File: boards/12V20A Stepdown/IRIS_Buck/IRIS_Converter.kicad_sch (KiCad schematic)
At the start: 27 parts, among them J1 TB005-762-02BE, J2 TB005-762-02BE, Q1 CSD17571Q2, Q2 CSD16340Q3, U1 LM25145RGYR

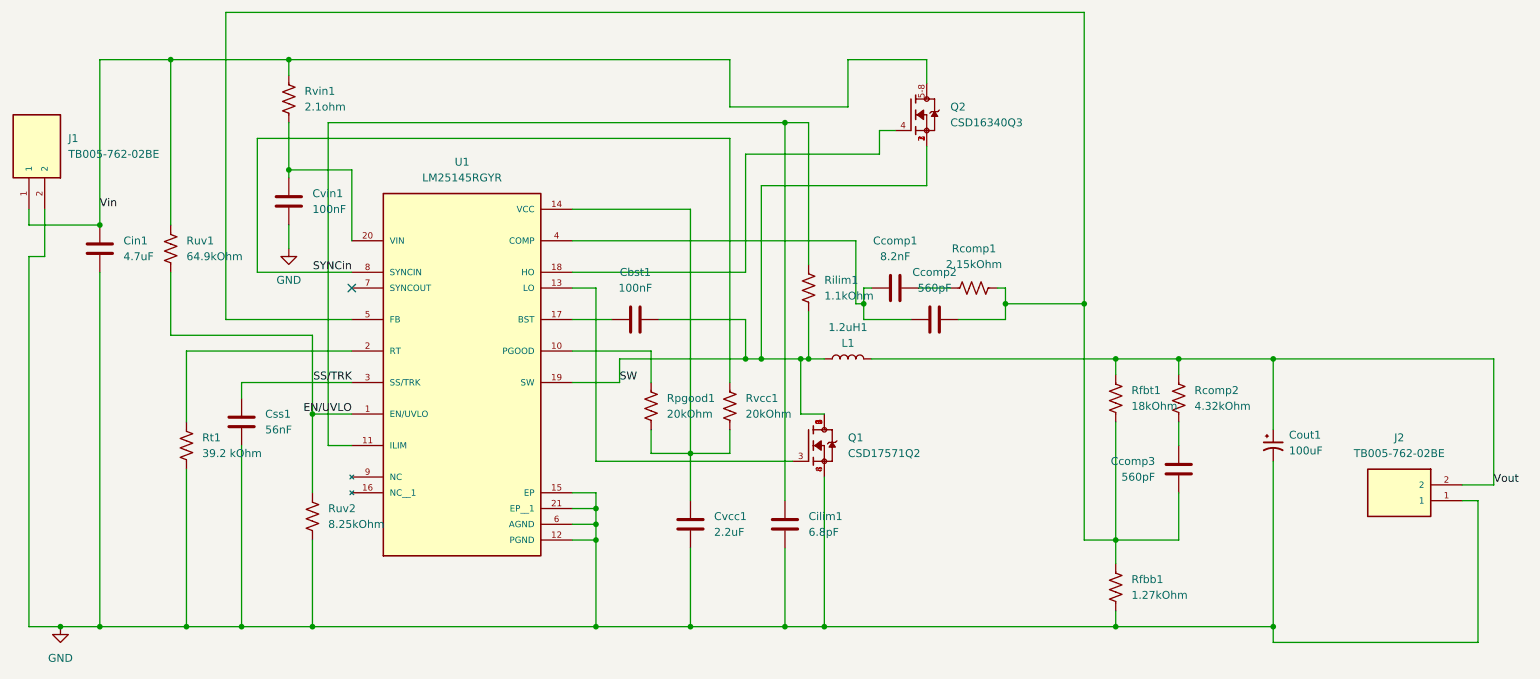
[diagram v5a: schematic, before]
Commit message: 10a stepdown and 20a stepdown update
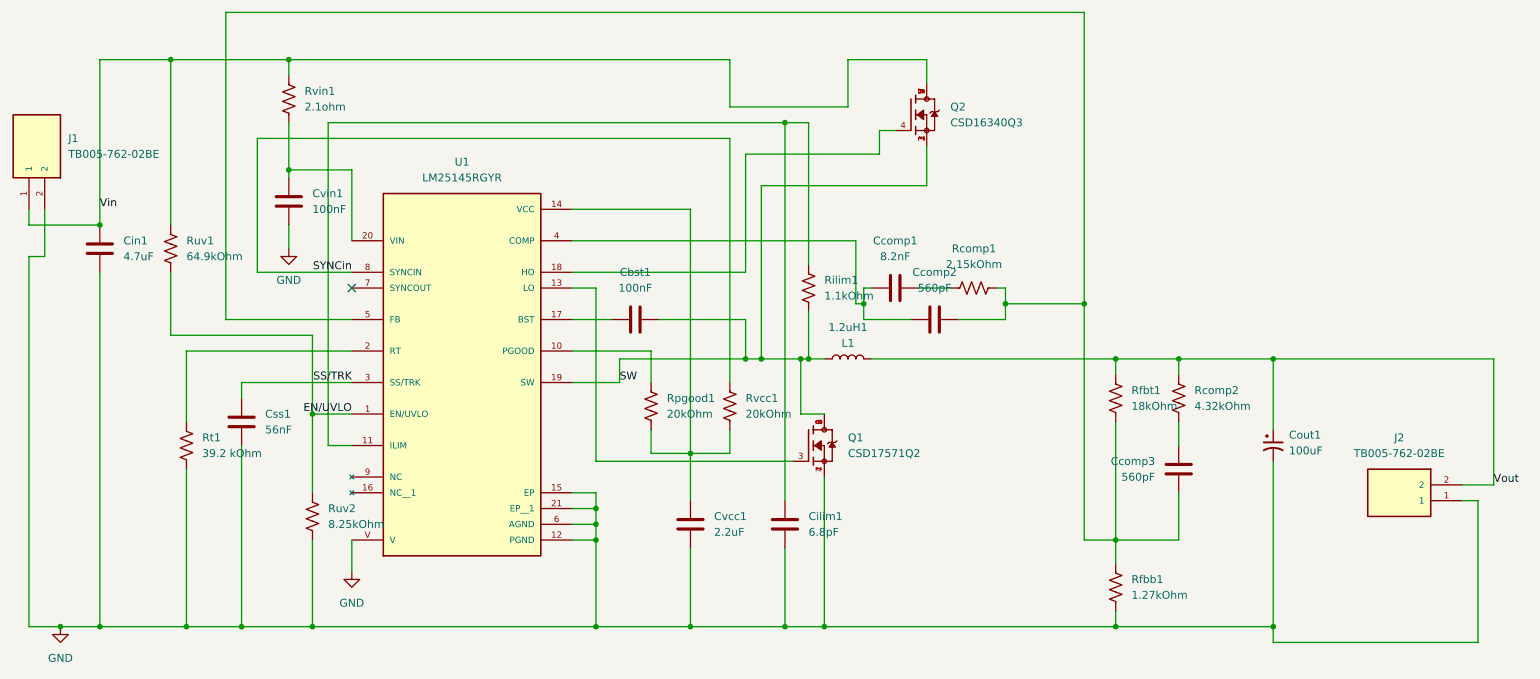
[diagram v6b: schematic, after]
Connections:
- net GND: now also Q1.7, U1.V; no longer Q1.8
- net SW: now also Q1.8; no longer Q1.7
- net Vin: now also Q2.5, Q2.6, Q2.7, Q2.8, Q2.9, Q2.V; no longer Q2.5-8
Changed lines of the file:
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@@
+	(wire
+		(pts
+			(xy 77.47 133.35) (xy 77.47 138.43)
+		)
+		(stroke
+			(width 0)
+			(type default)
+		)
+	)
 	(wire
 		(pts
@@
 		(pin "4"
 		)
-		(pin "5-8"
+		(pin "6"
+		)
+		(pin "5"
+		)
+		(pin "8"
+		)
+		(pin "7"
+		)
+		(pin "V"
+		)
+		(pin "9"
 		)
 		(instances
@@
 		(pin "21"
 		)
+		(pin "V"
+		)
 		(instances
 			(project ""
@@
 					(unit 1)
 				)
+			)
+		)
+	)
+	(symbol
+		(lib_id "power:GND")
+		(at 77.47 138.43 0)
+		(unit 1)
+		(exclude_from_sim no)
+		(in_bom yes)
+		(on_board yes)
+		(dnp no)
+		(fields_autoplaced yes)
+		(property "Reference" "#PWR03"
+			(at 77.47 144.78 0)
+			(effects
+				(font
+					(size 1.27 1.27)
+				)
+				(hide yes)
+			)
+		)
+		(property "Value" "GND"
+			(at 77.47 143.51 0)
+			(effects
+				(font
+					(size 1.27 1.27)
+				)
+			)
+		)
+		(property "Footprint" ""
+			(at 77.47 138.43 0)
+			(effects
+				(font
+					(size 1.27 1.27)
+				)
+				(hide yes)
+			)
+		)
+		(property "Datasheet" ""
+			(at 77.47 138.43 0)
+			(effects
+				(font
+					(size 1.27 1.27)
+				)
+				(hide yes)
+			)
+		)
+		(property "Description" "Power symbol creates a global label with name \"GND\" , ground"
+			(at 77.47 138.43 0)
+			(effects
+				(font
+					(size 1.27 1.27)
+				)
+				(hide yes)
+			)
+		)
+		(pin "1"
+		)
+		(instances
+			(project "IRIS_Converter"
+				(path "/1513ce43-e5f2-482b-99a2-cdd75b9aa1c1"
+					(reference "#PWR03")
+					(unit 1)
+				)
